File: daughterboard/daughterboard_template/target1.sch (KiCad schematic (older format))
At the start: 0 parts

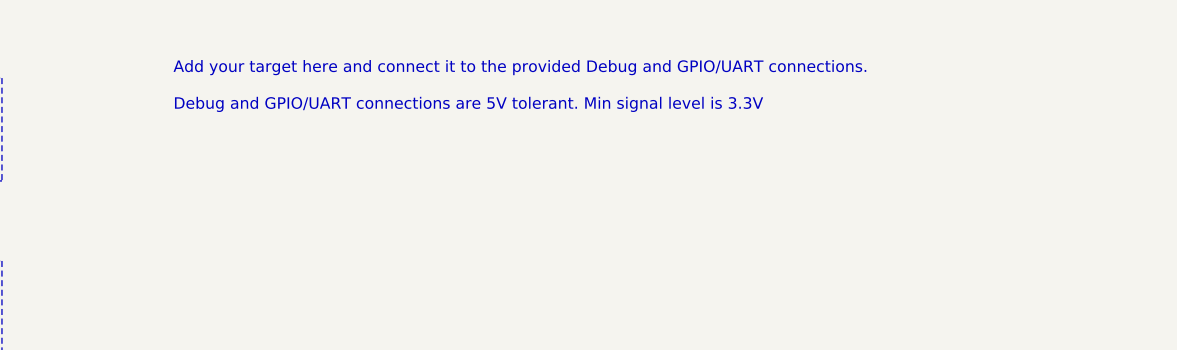
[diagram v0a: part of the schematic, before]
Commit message: updated LED resistor values, updated partlists, minor change to daughterboard template
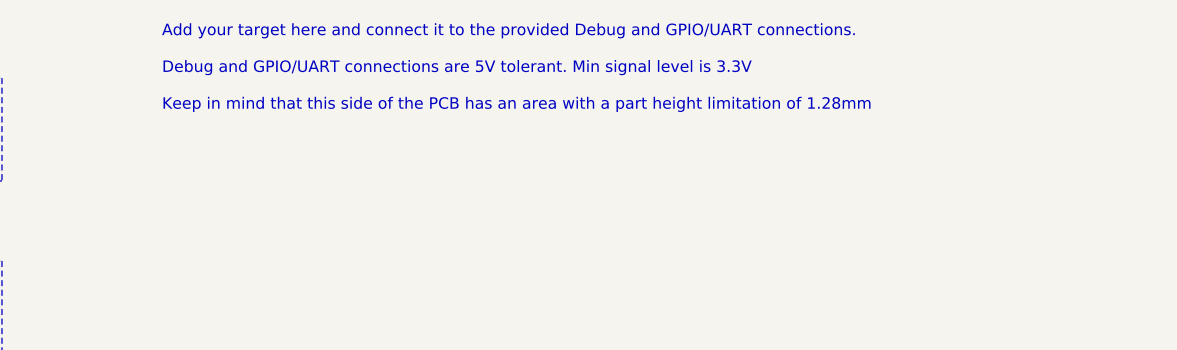
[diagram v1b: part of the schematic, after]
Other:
- note added: "Add your target here and connect it to the provided Debug and GPIO/UART connections.\n\nDebug and GPIO/UART connections are 5V tolerant. Min signal level is 3.3V\n\nKeep in mind that this side of the PCB has an area with a part height limitation of 1.28mm"
- note removed: "Add your target here and connect it to the provided Debug and GPIO/UART connections.\n\nDebug and GPIO/UART connections are 5V tolerant. Min signal level is 3.3V"
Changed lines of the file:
@@
 Text Notes 1100 750  0    50   ~ 0
 Power
-Text Notes 2450 950  0    50   ~ 0
-Add your target here and connect it to the provided Debug and GPIO/UART connections.\n\nDebug and GPIO/UART connections are 5V tolerant. Min signal level is 3.3V
+Text Notes 2400 950  0    50   ~ 0
+Add your target here and connect it to the provided Debug and GPIO/UART connections.\n\nDebug and GPIO/UART connections are 5V tolerant. Min signal level is 3.3V\n\nKeep in mind that this side of the PCB has an area with a part height limitation of 1.28mm
 $EndSCHEMATC
